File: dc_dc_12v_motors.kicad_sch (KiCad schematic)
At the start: 18 parts, among them Q7 CSD17505Q5A, Q8 CSD18540Q5B, U9 LM3150MH

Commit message: updated LCSC component names based on the availability, keepout zones for MCU gnd pins, added thermals to copper zones
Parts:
- C43: LCSC (none) -> C128514
- C44: LCSC (none) -> C90143
- L1: LCSC C2976965 -> C357285
- Q7: LCSC (none) -> C553150
- Q8: LCSC (none) -> C86513
- R38: LCSC (none) -> C483204
- R39: LCSC (none) -> C228358
- R40: LCSC (none) -> C482962
- R41: LCSC (none) -> C84376
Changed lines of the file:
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@@
+      (effects (font (size 1.27 1.27)) hide)
+    )
+    (property "LCSC" "C128514" (id 4) (at 222.885 95.25 0)
       (effects (font (size 1.27 1.27)) hide)
     )
@@
       (effects (font (size 1.27 1.27)) hide)
     )
-    (property "Datasheet" "https://datasheet.lcsc.com/lcsc/2202241530_SXN-Shun-Xiang-Nuo-Elec-SMMS1770-4R7M_C2976965.pdf" (id 3) (at 184.785 91.44 0)
-      (effects (font (size 1.27 1.27)) hide)
-    )
-    (property "LCSC" "C2976965" (id 4) (at 184.785 91.44 0)
+    (property "Datasheet" "https://datasheet.lcsc.com/lcsc/2009171440_TAI-TECH-TMPC1707HP-4R7MG-D_C357285.pdf" (id 3) (at 184.785 91.44 0)
+      (effects (font (size 1.27 1.27)) hide)
+    )
+    (property "LCSC" "C357285" (id 4) (at 184.785 91.44 0)
       (effects (font (size 1.27 1.27)) hide)
     )
@@
       (effects (font (size 1.27 1.27)) hide)
     )
-    (property "Datasheet" "~" (id 3) (at 160.655 96.52 0)
+    (property "Datasheet" "https://datasheet.lcsc.com/lcsc/2007151235_YAGEO-RC0805FR-071K43L_C482962.pdf" (id 3) (at 160.655 96.52 0)
+      (effects (font (size 1.27 1.27)) hide)
+    )
+    (property "LCSC" "C482962" (id 4) (at 160.655 96.52 90)
       (effects (font (size 1.27 1.27)) hide)
     )
@@
       (effects (font (size 1.27 1.27)) (justify left) hide)
     )
+    (property "LCSC" "C553150" (id 4) (at 175.895 83.82 0)
+      (effects (font (size 1.27 1.27)) hide)
+    )
     (pin "1")
     (pin "2")
@@
       (effects (font (size 1.27 1.27)) hide)
     )
-    (property "Datasheet" "https://ee.farnell.com/taiyo-yuden/emk325abj107mm-t/cap-100-f-16v-20-x5r-1210/dp/2309033?st=2309033" (id 3) (at 236.855 95.25 0)
+    (property "Datasheet" "https://datasheet.lcsc.com/lcsc/1912111437_Taiyo-Yuden-EMK325ABJ107MM-P_C90143.pdf" (id 3) (at 236.855 95.25 0)
+      (effects (font (size 1.27 1.27)) hide)
+    )
+    (property "LCSC" "C90143" (id 4) (at 236.855 95.25 0)
       (effects (font (size 1.27 1.27)) hide)
     )
@@
       (effects (font (size 1.27 1.27)) hide)
     )
-    (property "Datasheet" "~" (id 3) (at 127.635 93.98 0)
+    (property "Datasheet" "https://datasheet.lcsc.com/lcsc/2007151311_YAGEO-RC0805FR-07604KL_C483204.pdf" (id 3) (at 127.635 93.98 0)
+      (effects (font (size 1.27 1.27)) hide)
+    )
+    (property "LCSC" "C483204" (id 4) (at 127.635 93.98 90)
       (effects (font (size 1.27 1.27)) hide)
     )
@@
       (effects (font (size 1.27 1.27)) hide)
     )
-    (property "Datasheet" "~" (id 3) (at 208.915 95.25 0)
+    (property "Datasheet" "https://datasheet.lcsc.com/lcsc/1810311323_YAGEO-AC0805FR-07191KL_C228358.pdf" (id 3) (at 208.915 95.25 0)
+      (effects (font (size 1.27 1.27)) hide)
+    )
+    (property "LCSC" "C228358" (id 4) (at 208.915 95.25 0)
       (effects (font (size 1.27 1.27)) hide)
     )
@@
       (effects (font (size 1.27 1.27)) (justify left) hide)
     )
+    (property "LCSC" "C86513" (id 4) (at 175.895 101.6 0)
+      (effects (font (size 1.27 1.27)) hide)
+    )
     (pin "1")
     (pin "2")
@@
       (effects (font (size 1.27 1.27)) hide)
     )
-    (property "Datasheet" "~" (id 3) (at 208.915 102.87 0)
-      (effects (font (size 1.27 1.27)) hide)
-    )
+    (property "Datasheet" "https://datasheet.lcsc.com/lcsc/1810201611_YAGEO-RC0805FR-0710KL_C84376.pdf" (id 3) (at 208.915 102.87 0)
+      (effects (font (size 1.27 1.27)) hide)
+    )
+    (property "LCSC" "C84376" (id 4) (at 208.915 102.87 0)
+      (effects (font (size 1.27 1.27)) hide)
+    )

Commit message: more 'LCSC' fields in sch files changed to 'LCSC Part'
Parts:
- C37: LCSC C49678 -> (none); LCSC Part (none) -> C49678
- C38, C39, C40: LCSC C189474 -> (none); LCSC Part (none) -> C189474
- C41: LCSC C13967 -> (none); LCSC Part (none) -> C13967
- C42: LCSC C1743 -> (none); LCSC Part (none) -> C1743
- C43: LCSC C128514 -> (none); LCSC Part (none) -> C128514
- C44: LCSC C90143 -> (none); LCSC Part (none) -> C90143
- C45: LCSC C49217 -> (none); LCSC Part (none) -> C49217
- C46: LCSC C1596 -> (none); LCSC Part (none) -> C1596
- L1: LCSC C357285 -> (none); LCSC Part (none) -> C357285
- Q7: LCSC C553150 -> (none); LCSC Part (none) -> C553150
- Q8: LCSC C86513 -> (none); LCSC Part (none) -> C86513
- R38: LCSC C483204 -> (none); LCSC Part (none) -> C483204
- R39: LCSC C228358 -> (none); LCSC Part (none) -> C228358
- R40: LCSC C482962 -> (none); LCSC Part (none) -> C482962
- R41: LCSC C84376 -> (none); LCSC Part (none) -> C84376
- U9: LCSC C48112 -> (none); LCSC Part (none) -> C48112
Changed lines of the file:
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@@
       (effects (font (size 1.27 1.27)) hide)
     )
-    (property "LCSC" "C128514" (id 4) (at 222.885 95.25 0)
+    (property "LCSC Part" "C128514" (id 4) (at 222.885 95.25 0)
       (effects (font (size 1.27 1.27)) hide)
     )
@@
       (effects (font (size 1.27 1.27)) hide)
     )
-    (property "LCSC" "C357285" (id 4) (at 184.785 91.44 0)
+    (property "LCSC Part" "C357285" (id 4) (at 184.785 91.44 0)
       (effects (font (size 1.27 1.27)) hide)
     )
@@
       (effects (font (size 1.27 1.27)) hide)
     )
-    (property "LCSC" "C13967" (id 4) (at 160.655 88.9 0)
+    (property "LCSC Part" "C13967" (id 4) (at 160.655 88.9 0)
       (effects (font (size 1.27 1.27)) hide)
     )
@@
       (effects (font (size 1.27 1.27)) hide)
     )
-    (property "LCSC" "C482962" (id 4) (at 160.655 96.52 90)
+    (property "LCSC Part" "C482962" (id 4) (at 160.655 96.52 90)
       (effects (font (size 1.27 1.27)) hide)
     )
@@
       (effects (font (size 1.27 1.27)) hide)
     )
-    (property "LCSC" "C49217" (id 4) (at 111.125 102.87 0)
+    (property "LCSC Part" "C49217" (id 4) (at 111.125 102.87 0)
       (effects (font (size 1.27 1.27)) hide)
     )
@@
       (effects (font (size 1.27 1.27)) hide)
     )
-    (property "LCSC" "C49678" (id 4) (at 60.325 82.55 0)
+    (property "LCSC Part" "C49678" (id 4) (at 60.325 82.55 0)
       (effects (font (size 1.27 1.27)) hide)
     )
@@
       (effects (font (size 1.27 1.27)) (justify left) hide)
     )
-    (property "LCSC" "C553150" (id 4) (at 175.895 83.82 0)
+    (property "LCSC Part" "C553150" (id 4) (at 175.895 83.82 0)
       (effects (font (size 1.27 1.27)) hide)
     )
@@
       (effects (font (size 1.27 1.27)) hide)
     )
-    (property "LCSC" "C90143" (id 4) (at 236.855 95.25 0)
+    (property "LCSC Part" "C90143" (id 4) (at 236.855 95.25 0)
       (effects (font (size 1.27 1.27)) hide)
     )
@@
       (effects (font (size 1.27 1.27)) hide)
     )
-    (property "LCSC" "C1743" (id 4) (at 197.485 93.98 0)
+    (property "LCSC Part" "C1743" (id 4) (at 197.485 93.98 0)
       (effects (font (size 1.27 1.27)) hide)
     )
@@
       (effects (font (size 1.27 1.27)) hide)
     )
-    (property "LCSC" "C483204" (id 4) (at 127.635 93.98 90)
+    (property "LCSC Part" "C483204" (id 4) (at 127.635 93.98 90)
       (effects (font (size 1.27 1.27)) hide)
     )
@@
       (effects (font (size 1.27 1.27)) hide)
     )
-    (property "LCSC" "C189474" (id 4) (at 74.295 82.55 0)
+    (property "LCSC Part" "C189474" (id 4) (at 74.295 82.55 0)
       (effects (font (size 1.27 1.27)) hide)
     )
@@
       (effects (font (size 1.27 1.27)) hide)
     )
-    (property "LCSC" "C189474" (id 4) (at 102.235 82.55 0)
+    (property "LCSC Part" "C189474" (id 4) (at 102.235 82.55 0)
       (effects (font (size 1.27 1.27)) hide)
     )
@@
       (effects (font (size 1.27 1.27)) hide)
     )
-    (property "LCSC" "C189474" (id 4) (at 89.535 82.55 0)
+    (property "LCSC Part" "C189474" (id 4) (at 89.535 82.55 0)
       (effects (font (size 1.27 1.27)) hide)
     )
@@
       (effects (font (size 1.27 1.27)) hide)
     )
-    (property "LCSC" "C228358" (id 4) (at 208.915 95.25 0)
+    (property "LCSC Part" "C228358" (id 4) (at 208.915 95.25 0)
       (effects (font (size 1.27 1.27)) hide)
     )
@@
       (effects (font (size 1.27 1.27)) hide)
     )
-    (property "LCSC" "C48112" (id 4) (at 144.145 93.98 0)
+    (property "LCSC Part" "C48112" (id 4) (at 144.145 93.98 0)
       (effects (font (size 1.27 1.27)) hide)
     )
@@
       (effects (font (size 1.27 1.27)) (justify left) hide)
     )
-    (property "LCSC" "C86513" (id 4) (at 175.895 101.6 0)
+    (property "LCSC Part" "C86513" (id 4) (at 175.895 101.6 0)
       (effects (font (size 1.27 1.27)) hide)
     )
@@
       (effects (font (size 1.27 1.27)) hide)
     )
-    (property "LCSC" "C1596" (id 4) (at 126.365 105.41 0)
+    (property "LCSC Part" "C1596" (id 4) (at 126.365 105.41 0)
       (effects (font (size 1.27 1.27)) hide)
     )
@@
       (effects (font (size 1.27 1.27)) hide)
     )
-    (property "LCSC" "C84376" (id 4) (at 208.915 102.87 0)
-      (effects (font (size 1.27 1.27)) hide)
-    )
+    (property "LCSC Part" "C84376" (id 4) (at 208.915 102.87 0)
+      (effects (font (size 1.27 1.27)) hide)
+    )

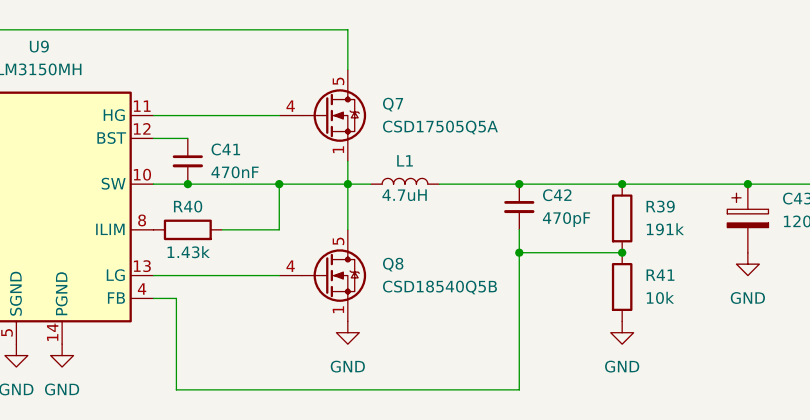
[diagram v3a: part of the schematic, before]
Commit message: Power circuit initial routing
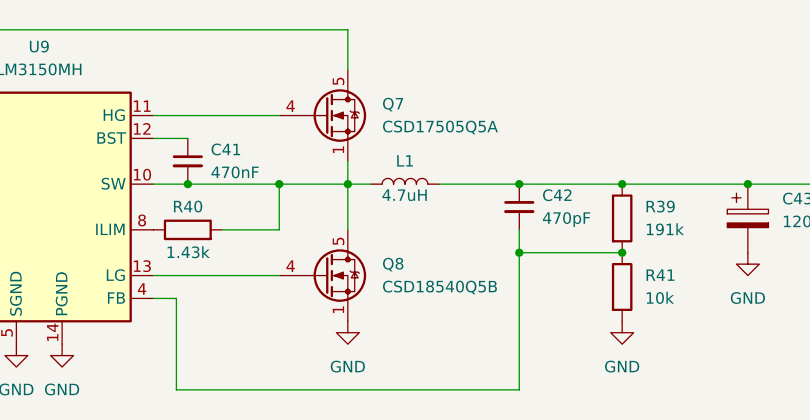
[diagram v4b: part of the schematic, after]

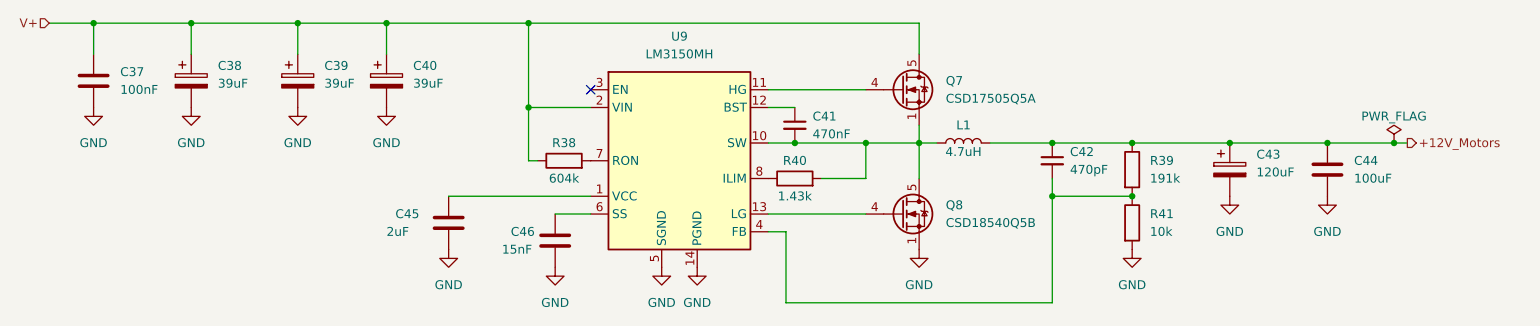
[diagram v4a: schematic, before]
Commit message: resolved align to grid warnings
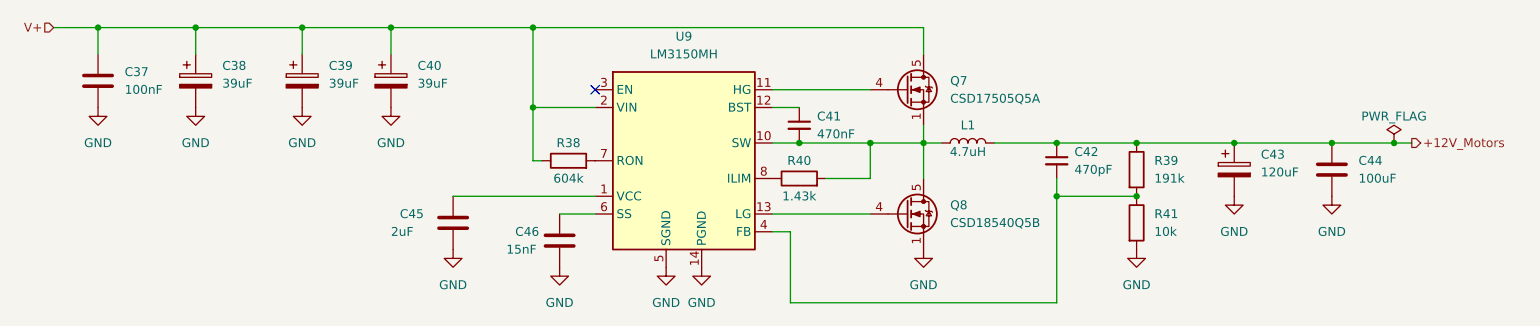
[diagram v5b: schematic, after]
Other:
- moved on the sheet: C37, C38, C39, C40, C41, C42, C43, C44, C45, C46, L1, Q7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

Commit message: adding lpf for current monitoring, resolved ERC-s in schematic
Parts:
- C45: value 2uF -> 2.2uF
- R41: footprint Resistor_SMD:R_0805_2012Metric_Pad1.20x1.40mm_HandSolder -> Resistor_SMD:R_0603_1608Metric; LCSC Part C84376 -> C25804
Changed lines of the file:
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@@
       (effects (font (size 1.27 1.27)) (justify left))
     )
-    (property "Value" "2uF" (at 102.87 104.14 0)
+    (property "Value" "2.2uF" (at 102.87 104.14 0)
       (effects (font (size 1.27 1.27)) (justify left))
     )
@@
       (effects (font (size 1.27 1.27)) hide)
     )
-    (property "Datasheet" "https://datasheet.lcsc.com/lcsc/1811101411_FH--Guangdong-Fenghua-Advanced-Tech-0805F225M500NT_C49217.pdf" (at 111.76 102.87 0)
+    (property "Datasheet" "https://datasheet.lcsc.com/lcsc/2304140030_FH--Guangdong-Fenghua-Advanced-Tech-0805F225M500NT_C49217.pdf" (at 111.76 102.87 0)
       (effects (font (size 1.27 1.27)) hide)
     )
@@
       (effects (font (size 1.27 1.27)) (justify left))
     )
-    (property "Footprint" "Resistor_SMD:R_0805_2012Metric_Pad1.20x1.40mm_HandSolder" (at 207.772 102.87 90)
-      (effects (font (size 1.27 1.27)) hide)
-    )
-    (property "Datasheet" "https://datasheet.lcsc.com/lcsc/1810201611_YAGEO-RC0805FR-0710KL_C84376.pdf" (at 209.55 102.87 0)
-      (effects (font (size 1.27 1.27)) hide)
-    )
-    (property "LCSC Part" "C84376" (at 209.55 102.87 0)
-      (effects (font (size 1.27 1.27)) hide)
-    )
+    (property "Footprint" "Resistor_SMD:R_0603_1608Metric" (at 207.772 102.87 90)
+      (effects (font (size 1.27 1.27)) hide)
+    )
+    (property "Datasheet" "https://datasheet.lcsc.com/lcsc/2206010045_UNI-ROYAL-Uniroyal-Elec-0603WAF1002T5E_C25804.pdf" (at 209.55 102.87 0)
+      (effects (font (size 1.27 1.27)) hide)
+    )
+    (property "LCSC Part" "C25804" (at 209.55 102.87 0)
+      (effects (font (size 1.27 1.27)) hide)
+    )

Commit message: optimized jlcpcb parts, replaced L4 inductor with FXL1360
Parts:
- C45: LCSC Part C49217 -> C377773
- L1: footprint Robotont:IND-SMD_L17.5-W17.5 -> Robotont:IND-FXL1360_12.6x13.5mm; LCSC Part C357285 -> C526021
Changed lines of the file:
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@@
       (effects (font (size 1.27 1.27)))
     )
-    (property "Footprint" "Robotont:IND-SMD_L17.5-W17.5" (at 185.42 91.44 0)
+    (property "Footprint" "Robotont:IND-FXL1360_12.6x13.5mm" (at 185.42 91.44 0)
       (effects (font (size 1.27 1.27)) hide)
     )
-    (property "Datasheet" "https://datasheet.lcsc.com/lcsc/2009171440_TAI-TECH-TMPC1707HP-4R7MG-D_C357285.pdf" (at 185.42 91.44 0)
+    (property "Datasheet" "https://datasheet.lcsc.com/lcsc/2305161118_cjiang--Changjiang-Microelectronics-Tech-FXL1360-4R7-M_C526021.pdf" (at 185.42 91.44 0)
       (effects (font (size 1.27 1.27)) hide)
     )
-    (property "LCSC Part" "C357285" (at 185.42 91.44 0)
+    (property "LCSC Part" "C526021" (at 185.42 91.44 0)
       (effects (font (size 1.27 1.27)) hide)
     )
@@
       (effects (font (size 1.27 1.27)) hide)
     )
-    (property "Datasheet" "https://datasheet.lcsc.com/lcsc/2304140030_FH--Guangdong-Fenghua-Advanced-Tech-0805F225M500NT_C49217.pdf" (at 111.76 102.87 0)
+    (property "Datasheet" "https://datasheet.lcsc.com/lcsc/2304140030_Samsung-Electro-Mechanics-CL21A225KBQNNNE_C377773.pdf" (at 111.76 102.87 0)
       (effects (font (size 1.27 1.27)) hide)
     )
-    (property "LCSC Part" "C49217" (at 111.76 102.87 0)
+    (property "LCSC Part" "C377773" (at 111.76 102.87 0)
       (effects (font (size 1.27 1.27)) hide)
     )
